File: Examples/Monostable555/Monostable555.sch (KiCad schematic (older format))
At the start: 11 parts, among them U2 plot_v1, U3 IC, U4 plot_v1, U5 plot_v1, X1 LM555N

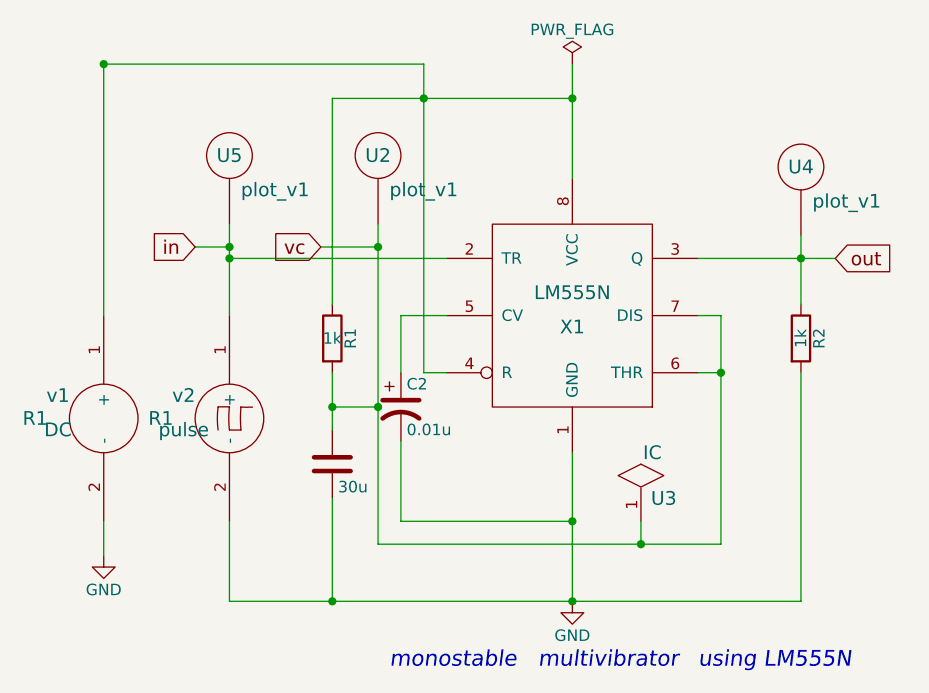
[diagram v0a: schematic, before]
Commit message: lm555 subcircuit modified
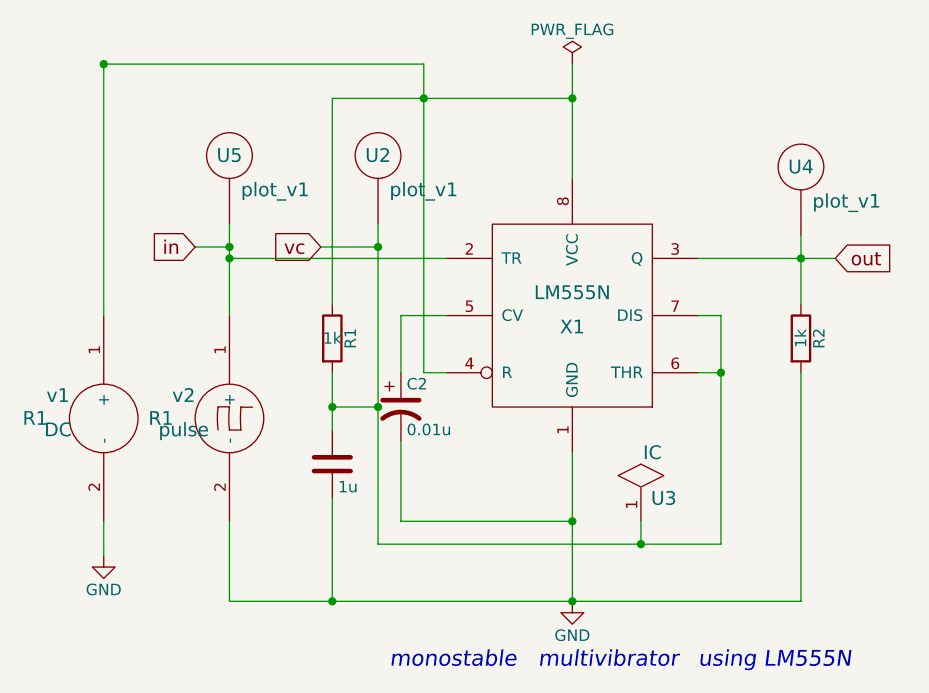
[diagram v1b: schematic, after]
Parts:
- C1: value 30u -> 1u
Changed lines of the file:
@@
 EESchema Schematic File Version 2
-LIBS:monostable555-rescue
 LIBS:adc-dac
 LIBS:memory
@@
 LIBS:eSim_Plot
 LIBS:eSim_Subckt
-LIBS:monostable555-cache
+LIBS:Monostable555-cache
 EELAYER 25 0
 EELAYER END
@@
 P 5150 3600
 F 0 "C1" H 5175 3700 50  0001 L CNN
-F 1 "30u" H 5175 3500 50  0000 L CNN
+F 1 "1u" H 5175 3500 50  0000 L CNN
 F 2 "" H 5188 3450 30  0000 C CNN
 F 3 "" H 5150 3600 60  0000 C CNN
